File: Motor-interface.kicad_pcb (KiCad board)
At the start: 2 copper layers, 100 x 110 mm, 73 parts, among them J101 CAN_PWR, J102 CAN_GND, J201 CAN, J202 CAN, P101 Motor Controller, P102 PSU_ISO, P103 Hall Phases, P104 LineContactor, P105 ReverseContactor, P106 FanContactor, P107 Battery+, P108 MC_USB, P109 MC_CAN, P110 HallCurrent, Q101 NJD35N04G, U101 1117_5v0, U102 1117_3v3, U103 TLP2361, U104 TLP2361, U105 TLP2361, U106 TLP2361, U107 TLP2361, U108 TLP2361, U109 Teensy_3.2, U110 TLP2361, U111 FODM3052, U201 TLP2361, U202 TLP2361, U203 MCP2551, U301 MCP4251, U302 TLP2361, U303 TLP2361, U304 TLP2361, U305 TLP2361, U306 TLP290-4

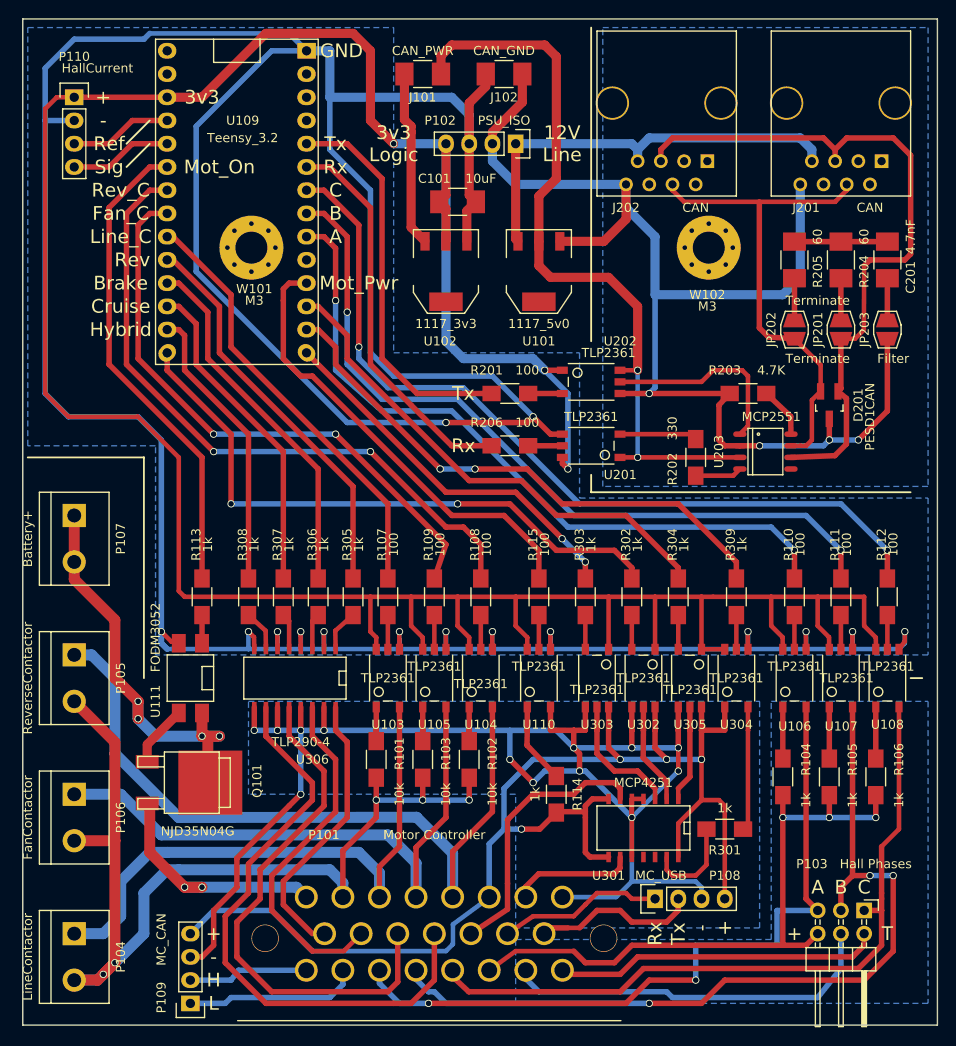
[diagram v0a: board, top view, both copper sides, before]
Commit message: adjusted via sized
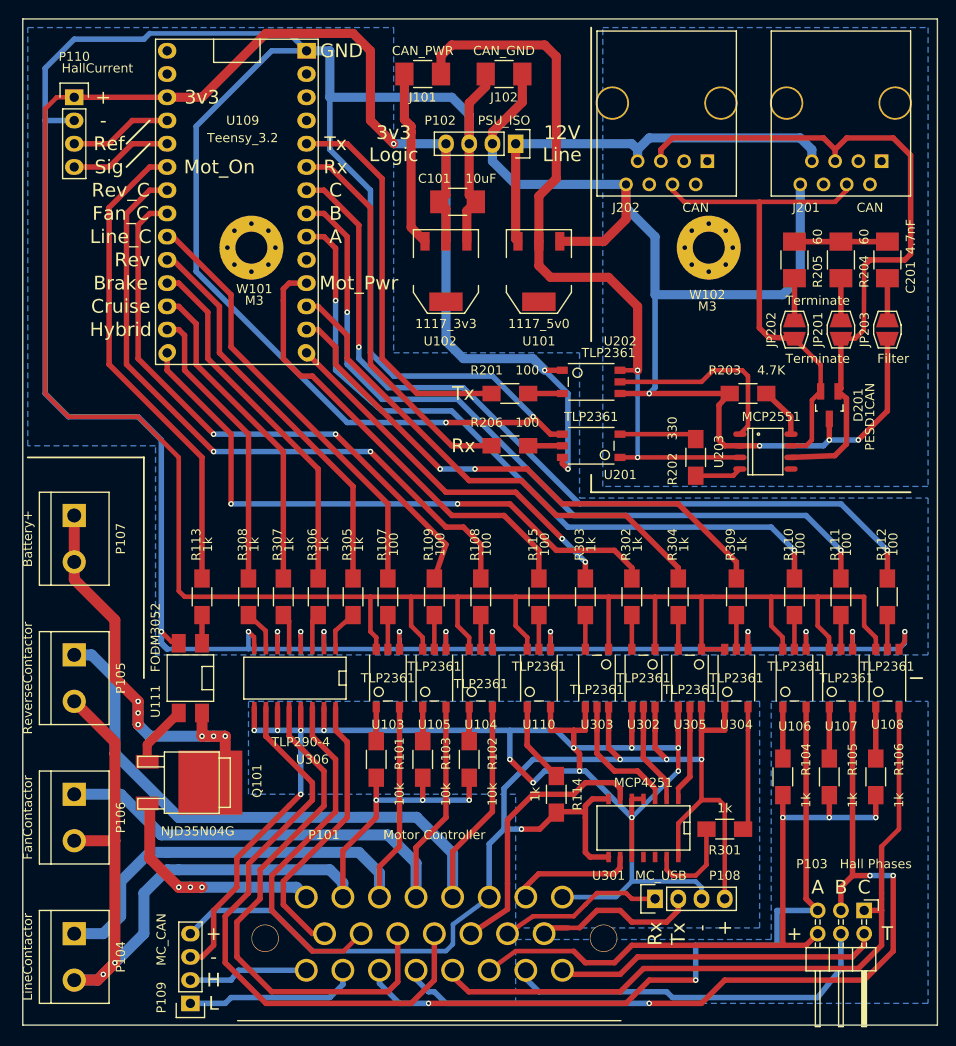
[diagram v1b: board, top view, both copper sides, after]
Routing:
- net /Battery+: track 47.0 -> 49.6 mm, vias 4 -> 6
- net /On/Off-Switch: track 27.1 -> 28.1 mm, vias 2 -> 3
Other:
- net class Default: via_drill 0.4 -> 0.3
- net class HT: via_drill 0.4 -> 0.3

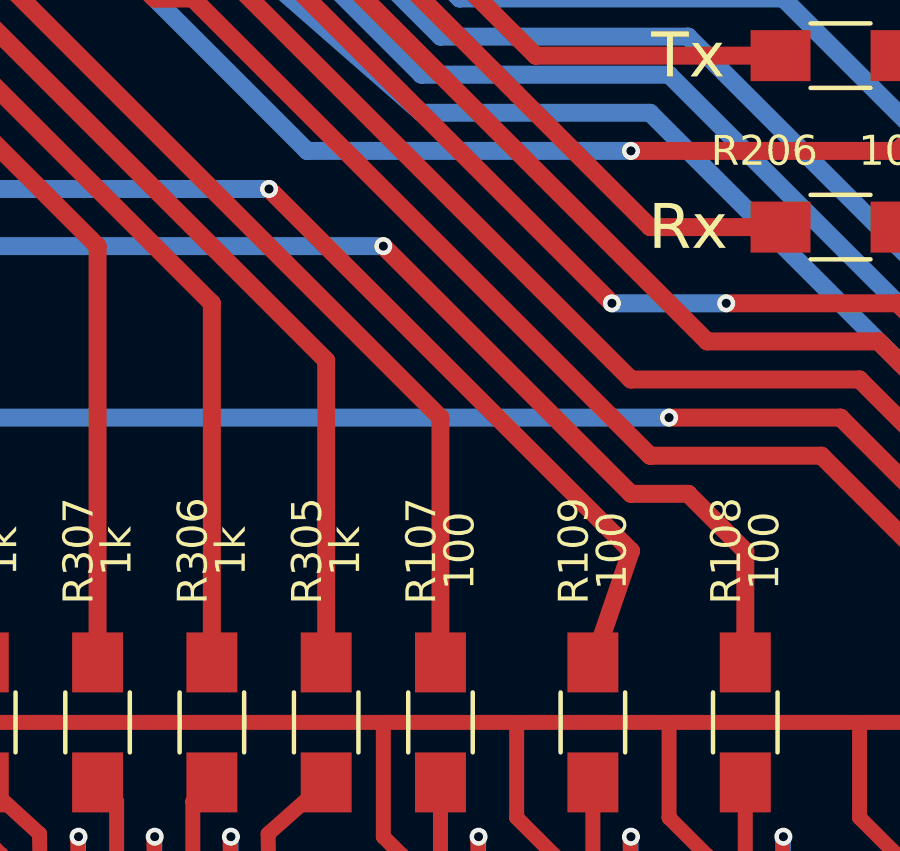
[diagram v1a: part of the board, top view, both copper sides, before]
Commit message: changed file extensions
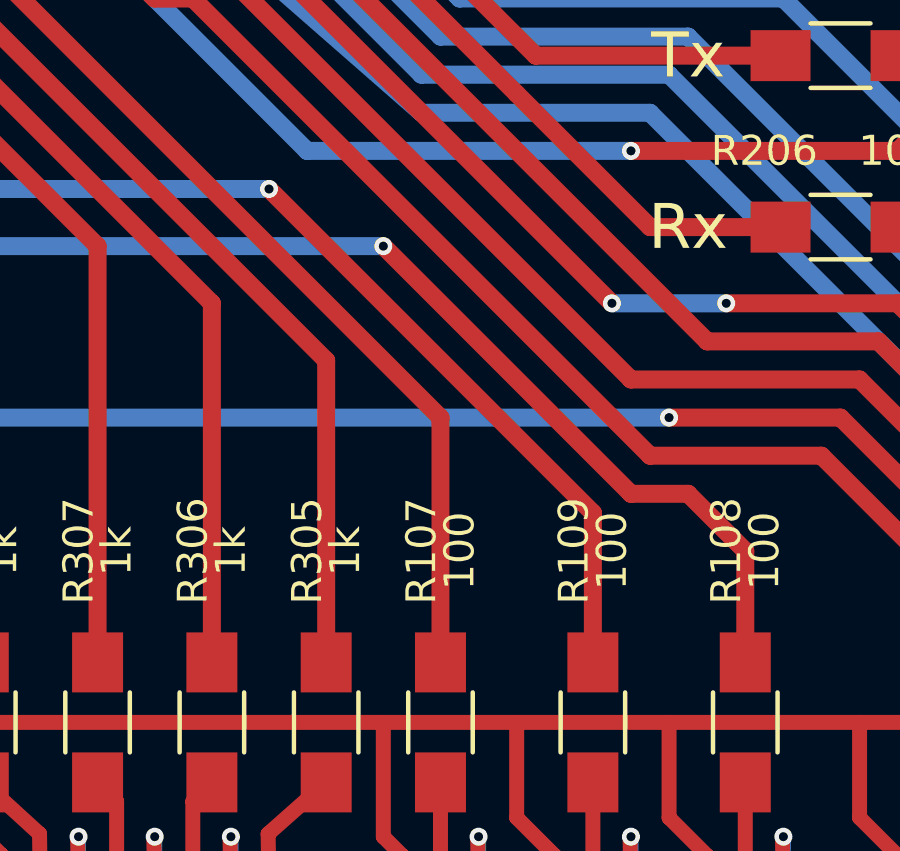
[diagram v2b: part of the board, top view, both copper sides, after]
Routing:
- net /Fan_Cont: track 64.3 -> 63.6 mm
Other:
- board text added: "BrettRD 2016 V3"
- board text removed: "BrettRD 2016 V1.0"
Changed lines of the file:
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@@
   )
   (setup
-    (last_trace_width 1.2)
+    (last_trace_width 0.5)
     (user_trace_width 0.5)
     (user_trace_width 0.6)
@@
     (pcbplotparams
       (layerselection 0x010f0_80000001)
-      (usegerberextensions false)
+      (usegerberextensions true)
       (excludeedgelayer true)
       (linewidth 0.200000)
@@
       (plotinvisibletext false)
       (padsonsilk false)
-      (subtractmaskfromsilk false)
+      (subtractmaskfromsilk true)
       (outputformat 1)
       (mirror false)
       (drillshape 0)
       (scaleselection 1)
-      (outputdirectory Motor-InterfaceV1/))
+      (outputdirectory Gerbers/))
   )
   (net 0 "")
@@
     (effects (font (size 1.5 1.5) (thickness 0.3)) (justify mirror))
   )
-  (gr_text "BrettRD 2016 V1.0" (at 102.9 124.015) (layer B.SilkS)
+  (gr_text "BrettRD 2016 V3" (at 102.9 124.015) (layer B.SilkS)
     (effects (font (size 1.5 1.5) (thickness 0.3)) (justify mirror))
   )
@@
   (via (at 81.945 108.775) (size 0.6) (drill 0.3) (layers F.Cu B.Cu) (net 39))
   (segment (start 94.01 130.39) (end 94.01 126.65) (width 0.5) (layer F.Cu) (net 40) (status 20))
-  (segment (start 90.2 118.935) (end 78.135 106.87) (width 0.6) (layer F.Cu) (net 41))
-  (segment (start 88.93 122.65) (end 90.2 118.935) (width 0.6) (layer F.Cu) (net 41))
+  (segment (start 88.93 117.665) (end 78.135 106.87) (width 0.6) (layer F.Cu) (net 41))
+  (segment (start 88.93 122.65) (end 88.93 117.665) (width 0.6) (layer F.Cu) (net 41) (status 400000))
   (segment (start 57.815 82.74) (end 59.72 82.74) (width 0.6) (layer F.Cu) (net 41))
   (segment (start 56.545 84.01) (end 57.815 82.74) (width 0.6) (layer F.Cu) (net 41))
